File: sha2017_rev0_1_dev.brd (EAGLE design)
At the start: 65 x 80 mm, 82 parts, among them IC1 CP210X_USB_UART, IC2 AP7215, IC32 ESP32_AI, Q1 MMBT2222A, Q2 MMBT2222A, Q6 MOSFET-NCHANNELBSS123LT1G, SW801 MCMT5-F-V, X701 2908-05WB-MG

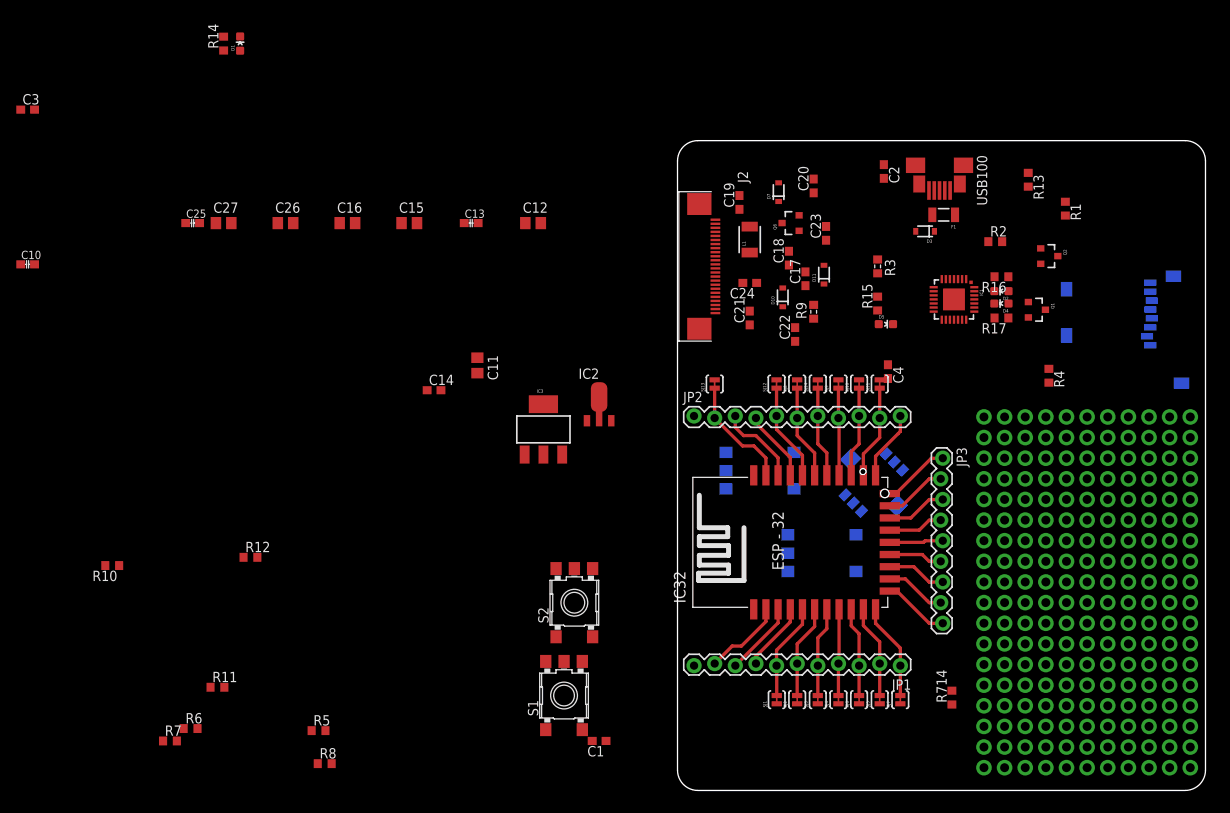
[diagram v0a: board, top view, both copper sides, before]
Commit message: removed dedicated flash switch, switch A will be now flash and switch A.
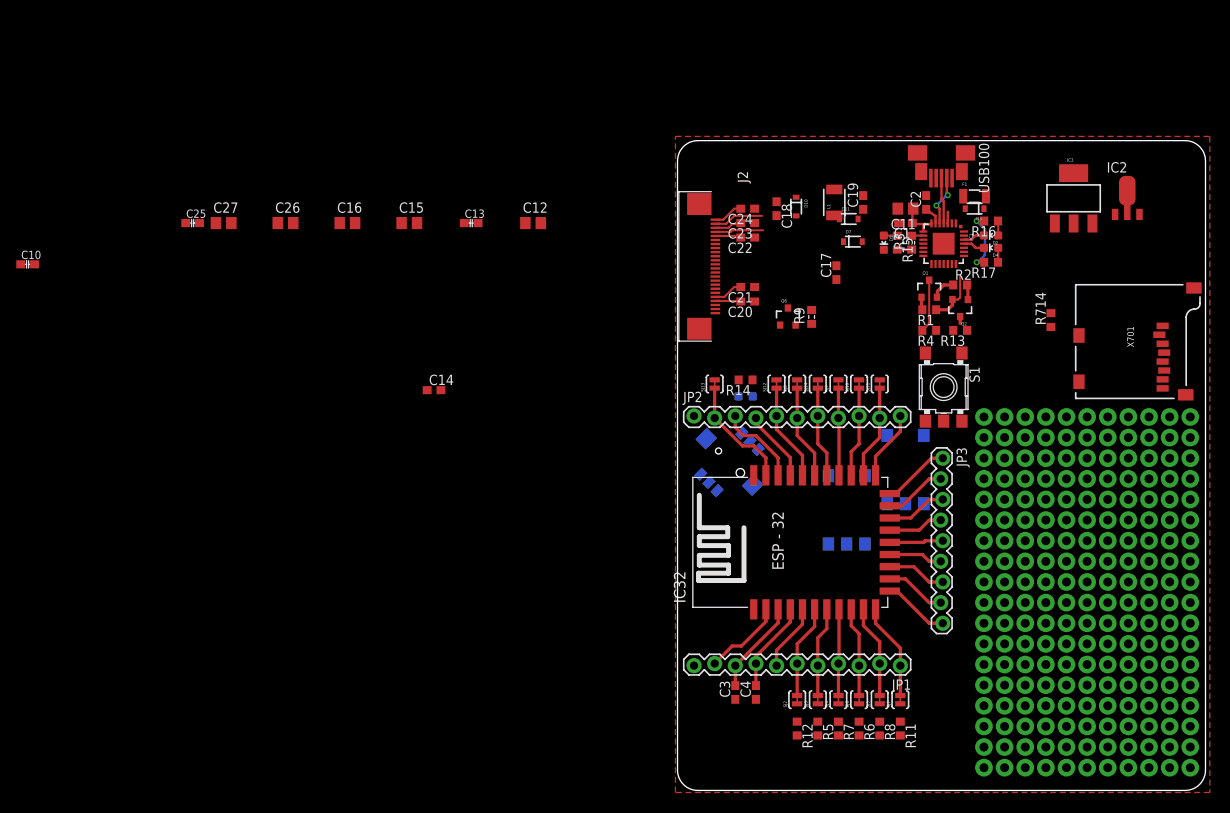
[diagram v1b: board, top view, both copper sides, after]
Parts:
- removed R10: 10k, rcl:R0603
- removed S2: SKHMPSE010, switch:SKHMPXE010
- removed SJ1: JUMPER-PAD-2-NC_BY_TRACE, SparkFun-Passives:PAD-JUMPER-2-NC_BY_TRACE_YES_SILK
- moved C3 112.9 mm to (7.11, 12.1), turned to 90 degrees
- moved R11 84.2 mm to (27.4, 7.62), turned to 270 degrees
- moved R7 82.3 mm to (19.8, 7.62), turned to 270 degrees
- moved R6 82.3 mm to (22.4, 7.62), turned to 270 degrees
- moved R14 76.4 mm to (8.38, 50.5), turned to 180 degrees
- moved D1 75.9 mm to (8.38, 48.5), flipped to the bottom, turned to 270 degrees
- moved C1 74.1 mm to (28.1, 69.8)
- moved IC3 71.2 mm to (48.8, 72.9)
- moved R12 70.5 mm to (14.7, 7.62), turned to 270 degrees
- moved IC2 69.8 mm to (55.4, 72.9)
- moved R8 68.5 mm to (24.9, 7.62), turned to 270 degrees
- moved R5 61.5 mm to (17.3, 7.62), turned to 270 degrees
- moved S1 60.2 mm to (32.8, 49.7), turned to 270 degrees
- moved C11 56.1 mm to (28.1, 71.6), turned to 180 degrees
- moved R714 48.1 mm to (46.0, 57.9)
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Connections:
- removed net BT_A: R10.1, S6.3, S6.4, SJ1.1
- net +3V3: no longer R10.2
- net ESP32_FLASH/TOUCHE_MENU: now also S6.3, S6.4; no longer S2.3, S2.4
- net GND: no longer S2.1, S2.2, S2.5
- net N$15: no longer SJ1.2
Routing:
- net VDD: track 0.00 -> 12.5 mm, vias 0 -> 2
- net ESP32_!RESET: track 9.95 -> 16.5 mm
- net N$11: track 0.00 -> 6.53 mm
- net USB_DN_CON: track 0.00 -> 6.42 mm, vias 0 -> 2
- net +5V: track 0.00 -> 6.28 mm
- net PREVGL: track 0.00 -> 6.15 mm
- net PREVGH: track 0.00 -> 5.96 mm
- net USB_DP_CON: track 0.00 -> 5.69 mm
- net VCOM: track 0.00 -> 3.69 mm
- net N$15: track 13.4 -> 9.76 mm
- net VGH: track 0.00 -> 3.62 mm
- net VGL: track 0.00 -> 3.51 mm
- net VSL: track 0.00 -> 3.36 mm
- net VSH: track 0.00 -> 3.20 mm
- net N$10: track 0.00 -> 3.03 mm
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- added copper zone on layer 1, net GND

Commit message: all parts places minor adjustments needed
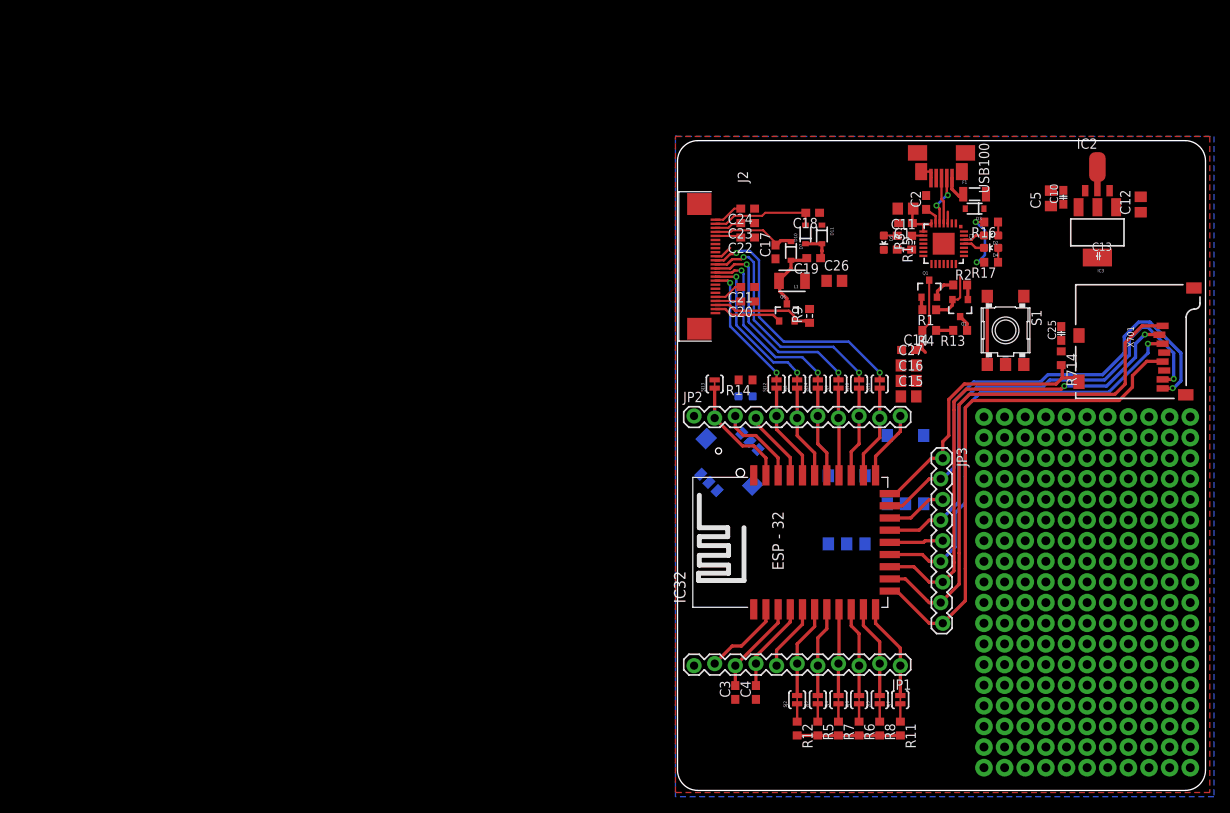
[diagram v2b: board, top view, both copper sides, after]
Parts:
- added C5: 100n, rcl:C0805
- moved C10 127.8 mm to (47.5, 73.0), turned to 90 degrees
- moved C25 107.8 mm to (47.2, 56.3), turned to 90 degrees
- moved C27 86.1 mm to (28.4, 52.3)
- moved C13 77.3 mm to (51.8, 65.8)
- moved C12 74.8 mm to (57.0, 72.1), turned to 90 degrees
- moved C16 71.8 mm to (28.4, 50.4)
- moved C26 67.9 mm to (19.3, 62.7)
- moved C15 65.1 mm to (28.4, 48.5)
- moved C14 58.6 mm to (28.4, 54.2)
- moved L1 11.0 mm to (14.1, 62.7), turned to 180 degrees
- moved S1 10.3 mm to (40.4, 56.6)
- moved C19 9.18 mm to (16.8, 65.5), turned to 180 degrees
- moved C17 7.91 mm to (12.1, 66.3)
- moved D7 7.71 mm to (14.0, 66.4), turned to 270 degrees
- moved IC3 5.11 mm to (51.7, 68.7), turned to 180 degrees
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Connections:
- net +5V: now also C5.1
- net GND: now also C5.2
- net LCD_!RESET: now also SJ8.2; no longer SJ12.2
- net LCD_BUSY: now also SJ12.2; no longer SJ14.2
- net LCD_CS: now also SJ9.2; no longer SJ11.2
- net LCD_D/!S: now also SJ14.2; no longer SJ8.2
- net LCD_MOSI: now also SJ11.2; no longer SJ9.2
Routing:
- net SD_DATA2: track 7.49 -> 64.8 mm
- net SD_CLK: track 8.17 -> 63.3 mm
- net SD_DATA0: track 6.78 -> 59.3 mm, vias 0 -> 1
- net SD_DATA3: track 7.31 -> 59.8 mm, vias 0 -> 2
- net SD_DATA1: track 7.64 -> 58.8 mm, vias 0 -> 1
- net SD_CMD: track 6.63 -> 55.0 mm, vias 0 -> 1
- net LCD_MOSI: track 0.00 -> 31.9 mm, vias 0 -> 2
- net LCD_SCK: track 0.00 -> 29.0 mm, vias 0 -> 2
- net SD_CD: track 8.78 -> 35.3 mm
- net LCD_CS: track 0.00 -> 25.8 mm, vias 0 -> 2
- net LCD_D/!S: track 0.00 -> 22.6 mm, vias 0 -> 2
- net LCD_!RESET: track 0.00 -> 19.4 mm, vias 0 -> 2
- net +3V3: track 8.57 -> 25.6 mm
- net LCD_BUSY: track 0.00 -> 16.2 mm, vias 0 -> 2
- net RESE: track 0.00 -> 12.8 mm
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- added copper zone on layer 16, net GND

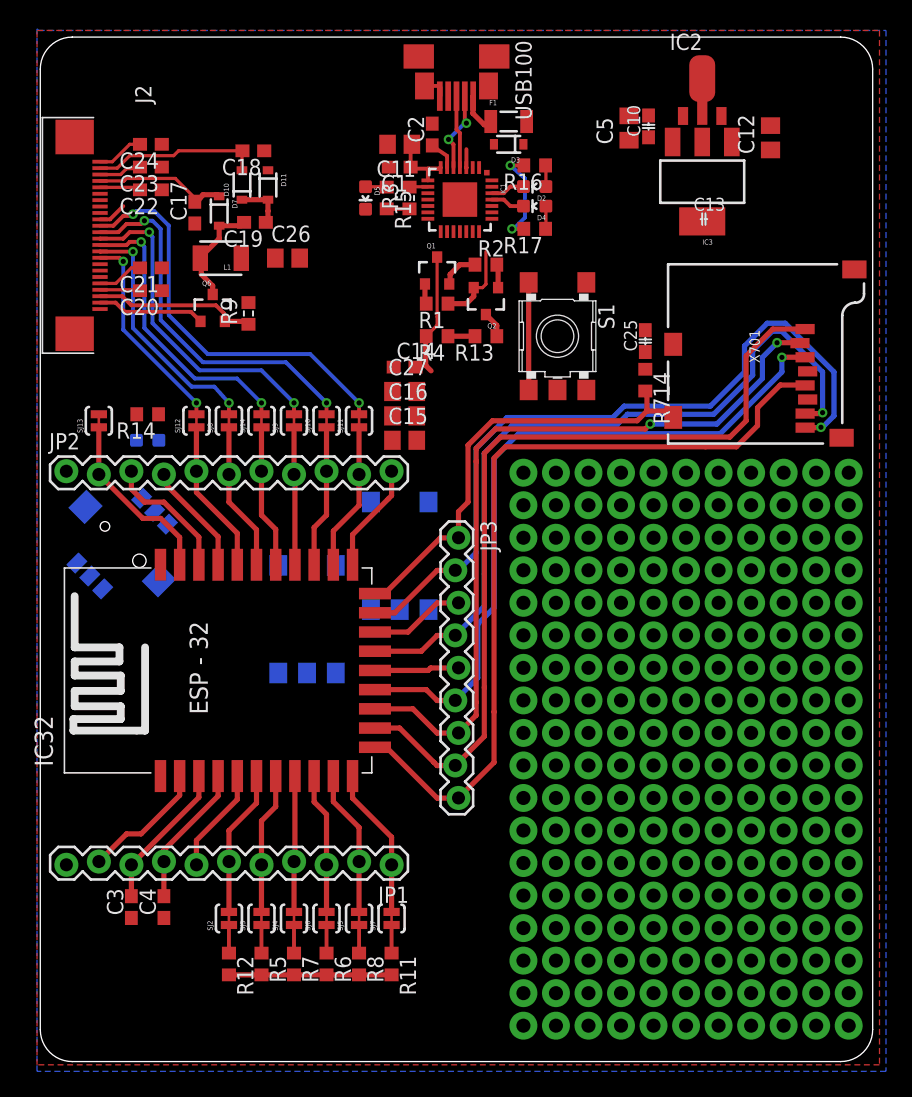
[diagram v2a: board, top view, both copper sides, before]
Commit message: finished routing. Part designators needs to be fixed
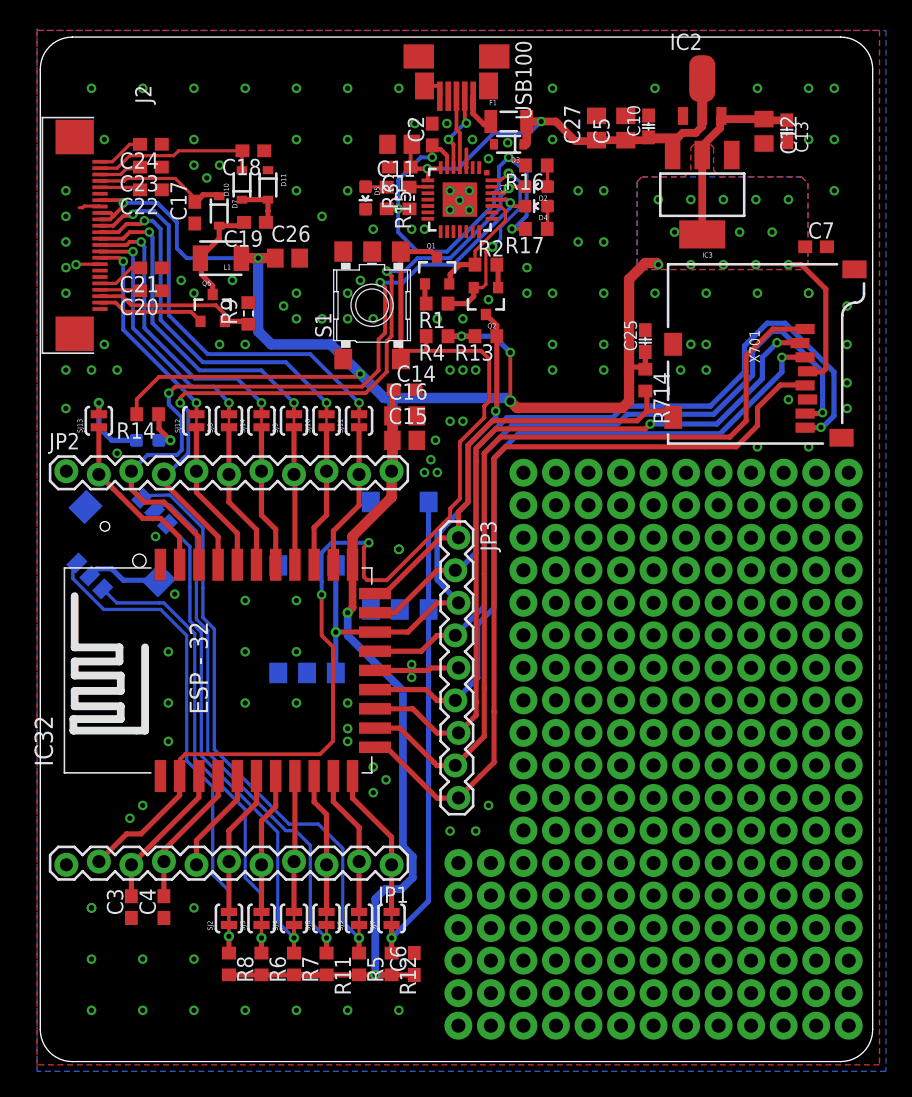
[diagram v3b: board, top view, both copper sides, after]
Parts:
- added C6, C7: 100n, rcl:C0603
- moved C27 25.5 mm to (43.4, 72.9), turned to 90 degrees
- moved S1 14.7 mm to (25.9, 59.1), turned to 90 degrees
- moved R12 12.7 mm to (27.4, 7.62)
- moved R8 10.2 mm to (14.7, 7.62)
- moved C13 9.43 mm to (58.3, 72.6), turned to 270 degrees
- moved R5 7.62 mm to (24.9, 7.62)
- moved R6 5.08 mm to (17.3, 7.62)
- moved R11 5.08 mm to (22.4, 7.62)
- moved C14 1.78 mm to (28.4, 52.5)
- moved IC3 1.02 mm to (51.7, 67.7)
- moved C12 0.72 mm to (56.5, 72.6), turned to 270 degrees
- moved C5 0.25 mm to (45.7, 72.9)
- moved D2 0.13 mm to (38.7, 68.3)
- moved D4 0.13 mm to (38.7, 66.8)
- moved R16 0.13 mm to (38.7, 70.0)
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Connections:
- removed net VCC: R714.1, X701.4
- net +3V3: now also C6.1, C7.1, R714.1, X701.4
- net BT_B: now also SJ7.1; no longer SJ2.1
- net BT_DOWN: now also SJ3.1; no longer SJ6.1
- net BT_MID: now also SJ6.1; no longer SJ7.1
- net BT_RIGHT: now also SJ2.1; no longer SJ5.1
- net BT_UP: now also SJ5.1; no longer SJ3.1
- net GND: now also C6.2, C7.2
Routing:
- net +3V3: track 25.6 -> 208.7 mm, vias 0 -> 21
- net ESP32_!RESET: track 27.8 -> 88.5 mm, vias 0 -> 2
- net ESP32_TX: track 13.1 -> 61.5 mm, vias 0 -> 3
- net ESP32_RX: track 11.5 -> 58.7 mm, vias 0 -> 3
- net BT_UP: track 2.20 -> 46.5 mm, vias 0 -> 1
- net BT_MID: track 2.20 -> 42.9 mm, vias 0 -> 1
- net +5V: track 6.28 -> 44.3 mm, vias 0 -> 2
- net BT_LEFT: track 2.20 -> 39.6 mm, vias 0 -> 1
- net BT_RIGHT: track 2.20 -> 39.1 mm, vias 0 -> 1
- net BT_B: track 2.20 -> 38.5 mm, vias 0 -> 1
- net ESP32_FLASH/TOUCHE_MENU: track 9.51 -> 44.6 mm, vias 0 -> 2
- net BT_DOWN: track 2.20 -> 36.7 mm, vias 0 -> 1
- net VDD: track 12.6 -> 38.0 mm, vias 2 -> 4
- net GND: track 10.1 -> 20.2 mm, vias 0 -> 143
- net N$11: track 6.53 -> 15.8 mm, vias 0 -> 2
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- added copper zone on layer 1, net +3V3
- added copper zone on layer 16, net +3V3
